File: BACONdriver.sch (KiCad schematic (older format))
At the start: 17 parts, among them P1 Batt_Mon, P2 Batt, P3 Motor, P4 Stearing, U1 ACS712_Mod, U2 VNH2SP30, U3 ACS712_Mod, U4 LM358, U5 Metro_Mini

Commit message: Changes to match prototype, adding an nRF24L01 for receiving control commands from the original transmitter and an FTDI style header for future expansion.
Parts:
- added JP1: JUMPER, Pin_Headers:Pin_Header_Straight_1x02, symbol JUMPER
- added P5: FTDI, Pin_Headers:Pin_Header_Straight_1x06, symbol CONN_01X06
- added U7: nRF24L01+, Pin_Headers:Pin_Header_Straight_2x04, symbol nRF24L01+
- P1: footprint (none) -> Pin_Headers:Pin_Header_Straight_1x04
- P2, P3: footprint (none) -> Pin_Headers:Pin_Header_Straight_1x02
- P4: footprint (none) -> Pin_Headers:Pin_Header_Straight_1x03; symbol CONN_01X05 -> CONN_01X03
- R1, R2, R3, R4, R5, R6, R7, R8: footprint (none) -> Resistors_ThroughHole:Resistor_Horizontal_RM10mm
- U1, U3: footprint (none) -> Pin_Headers:Pin_Header_Straight_1x03
- U2: footprint (none) -> Pin_Headers:Pin_Header_Straight_1x07
- U4: footprint (none) -> Housings_DIP:DIP-8_W7.62mm; symbol LM358 -> LM358-RESCUE-BACONdriver
- U5: footprint (none) -> BACONdriver:MetroMini
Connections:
- net labels added: +3V3, CTS, MISO, MOSI, NRF_CS, NRF_ENABLE, NRF_IRQ, RTS, RXD, SCK, STEAR, TXD
- net labels removed: +3.3V, PWD
- wire segments 49 -> 76
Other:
- moved on the sheet: U2

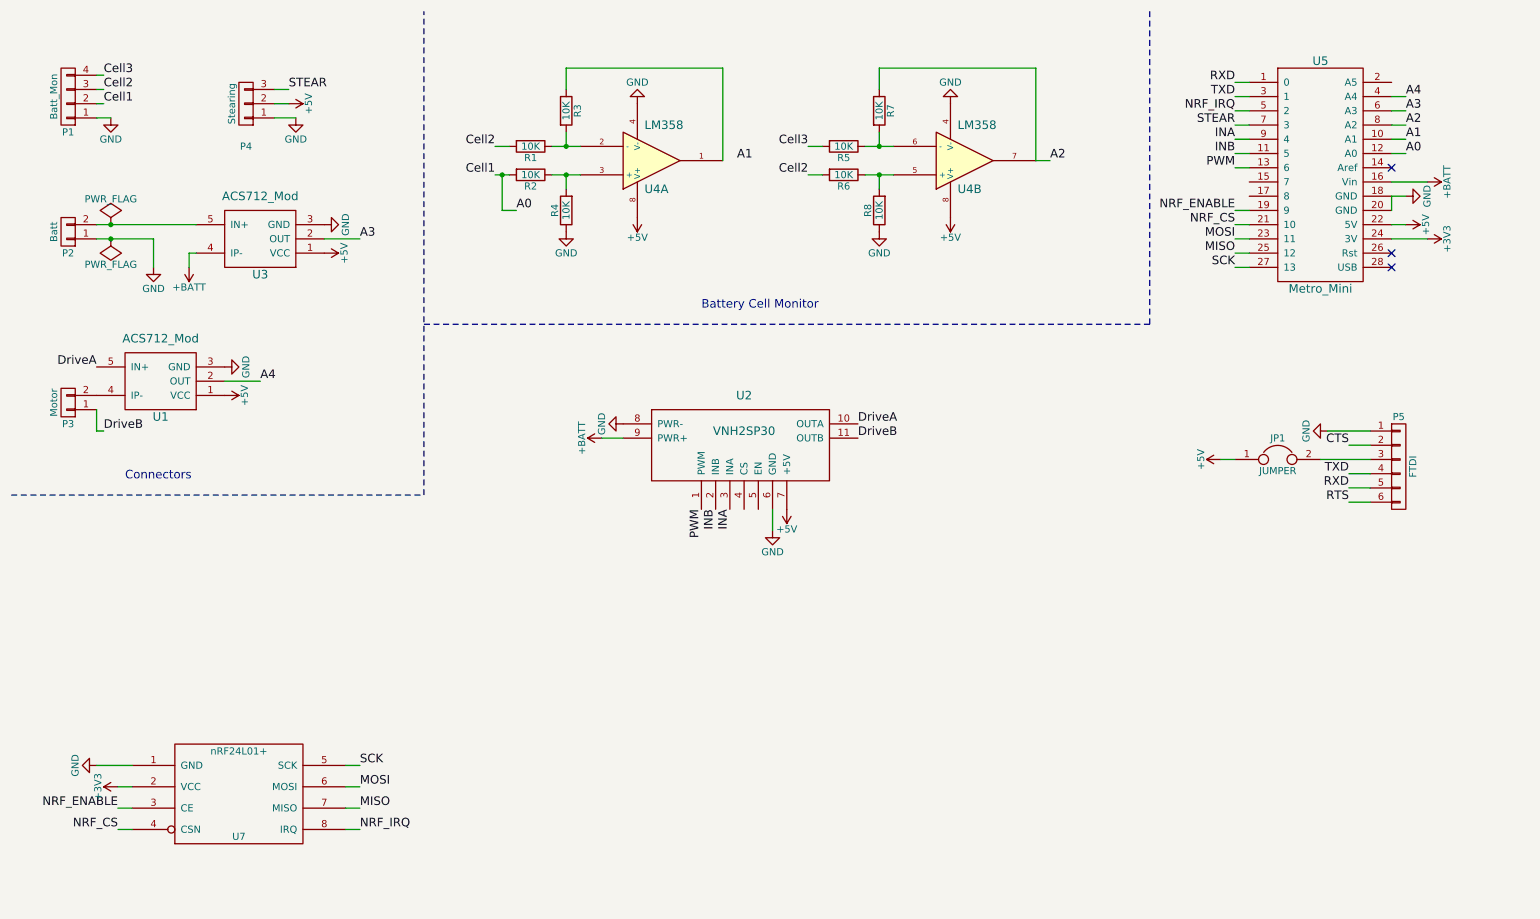
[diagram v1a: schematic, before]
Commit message: Various updates;  - Break out spare pins  - Use the motor driver CS for motor current (Current Sense not Chip Select)  - Allow the FTDI Vcc to be switched between 3.3v and 5v
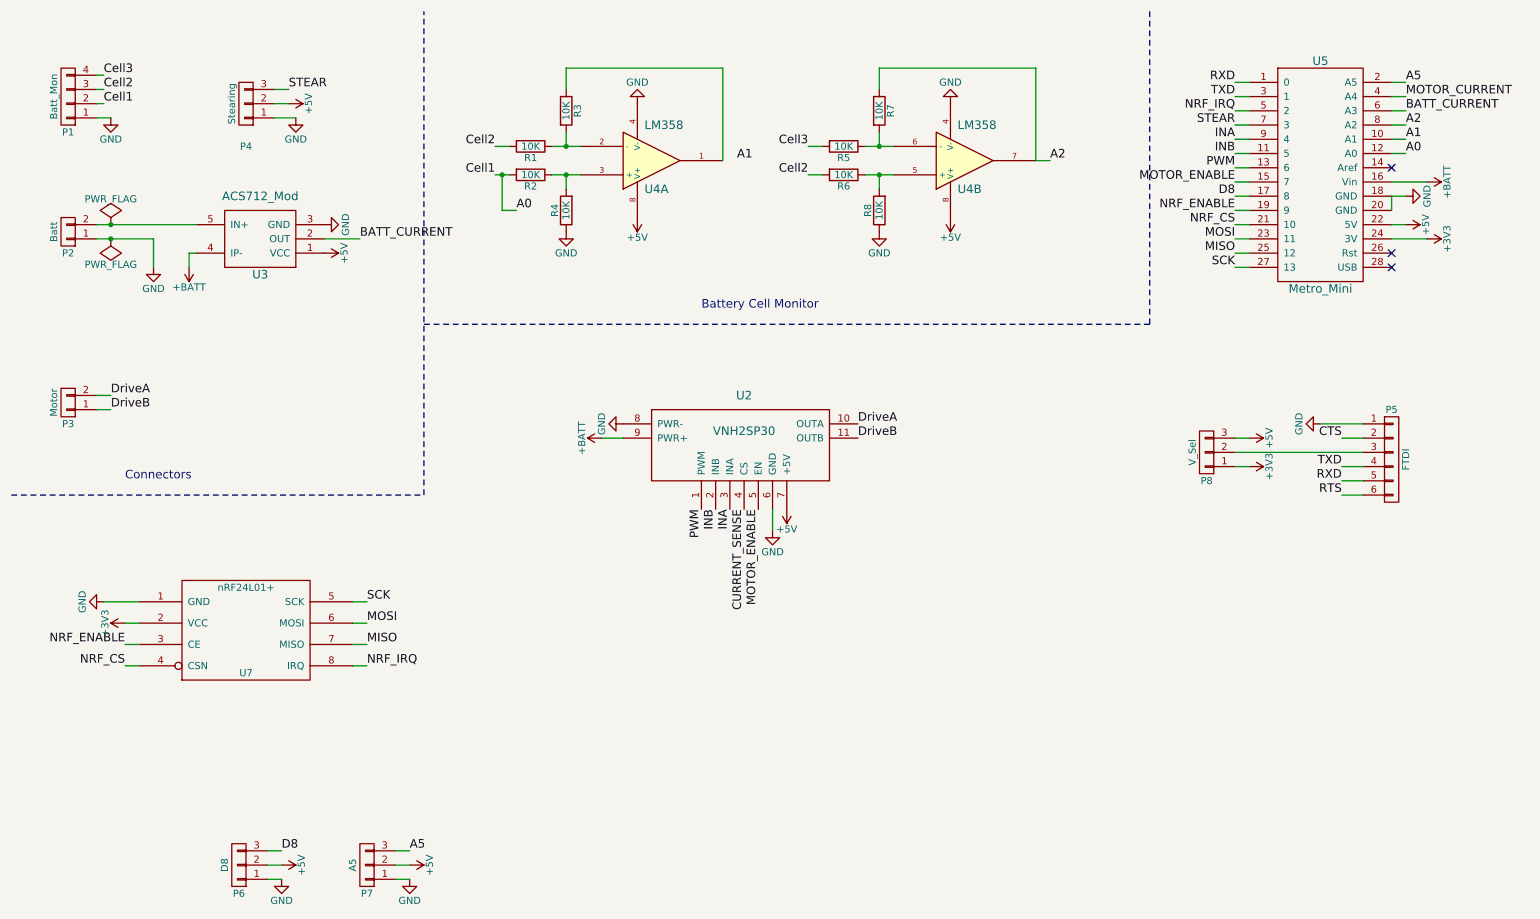
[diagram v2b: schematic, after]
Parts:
- removed JP1: JUMPER, Pin_Headers:Pin_Header_Straight_1x02, symbol JUMPER
- removed U1: ACS712_Mod, Pin_Headers:Pin_Header_Straight_1x03, symbol ACS712_Mod
- added P6: D8, Pin_Headers:Pin_Header_Straight_1x03, symbol CONN_01X03
- added P7: A5, Pin_Headers:Pin_Header_Straight_1x03, symbol CONN_01X03
- added P8: V_Sel, Pin_Headers:Pin_Header_Straight_1x03, symbol CONN_01X03
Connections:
- net +3V3: now also P8.1 (P1)
- net +5V: now also P6.2 (P2), P7.2 (P2), P8.3 (P3)
- net DriveA: now also P3.2 (P2)
- net GND: now also P6.1 (P1), P7.1 (P1)
- net MOTOR_ENABLE: now reaches U5.15 (7)
- net MOTOR_ENABLE: now also U2.5 (EN)
- net D8: now reaches U5.17 (8)
- net D8: now also P6.3 (P3)
- net A5: now reaches U5.2 (A5)
- net A5: now also P7.3 (P3)
- net CURRENT_SENSE: now reaches U2.4 (CS)
- net at P5.3 (P3): now also P8.2 (P2)
- net A3 renamed BATT_CURRENT
- net A4 renamed MOTOR_CURRENT
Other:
- moved on the sheet: P5, U7

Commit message: Moved the components that need laying out to a sub-sheet so the net list can be generated for just those components, while also maintaining the high level wiring
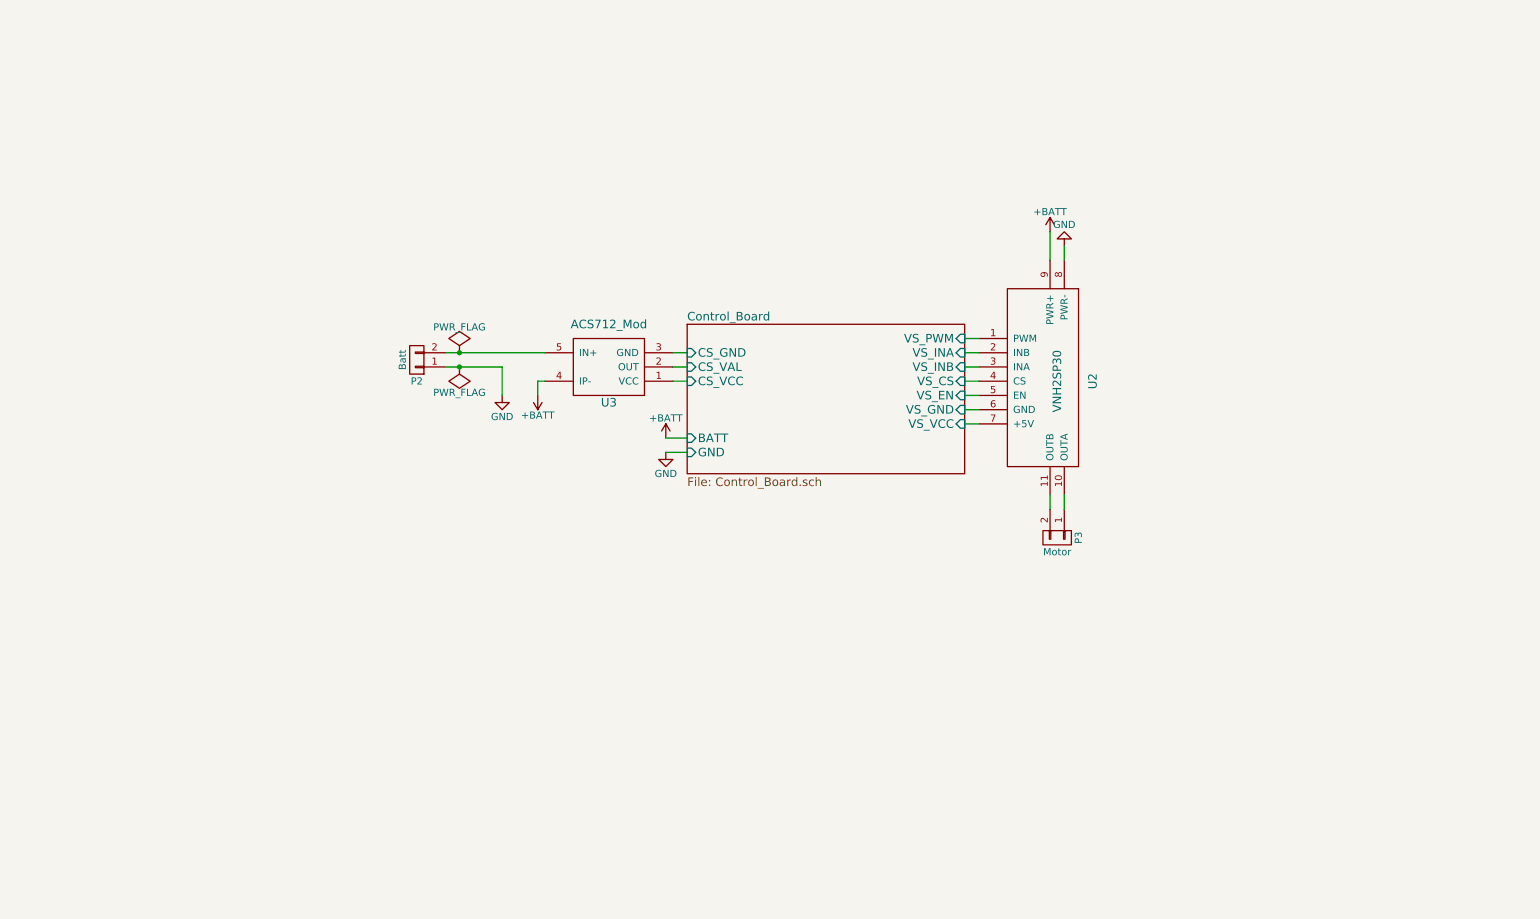
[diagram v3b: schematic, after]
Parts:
- removed P1: Batt_Mon, Pin_Headers:Pin_Header_Straight_1x04, symbol CONN_01X04
- removed P4: Stearing, Pin_Headers:Pin_Header_Straight_1x03, symbol CONN_01X03
- removed P5: FTDI, Pin_Headers:Pin_Header_Straight_1x06, symbol CONN_01X06
- removed P6: D8, Pin_Headers:Pin_Header_Straight_1x03, symbol CONN_01X03
- removed P7: A5, Pin_Headers:Pin_Header_Straight_1x03, symbol CONN_01X03
- removed P8: V_Sel, Pin_Headers:Pin_Header_Straight_1x03, symbol CONN_01X03
- removed R1, R2, R3, R4, R5, R6, R7, R8: 10K, Resistors_ThroughHole:Resistor_Horizontal_RM10mm, symbol R
- removed U4: LM358, Housings_DIP:DIP-8_W7.62mm, symbol LM358-RESCUE-BACONdriver
- removed U5: Metro_Mini, BACONdriver:MetroMini, symbol Metro_Mini
- removed U7: nRF24L01+, Pin_Headers:Pin_Header_Straight_2x04, symbol nRF24L01+
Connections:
- net GND: no longer U2.6 (GND), U3.3 (GND)
- net +5V renamed Control_Board/CS_VCC
- net Control_Board/CS_VCC: no longer U2.7 (+5V)
- net BATT_CURRENT renamed Control_Board/CS_VAL
- net CURRENT_SENSE renamed Control_Board/VS_CS
- net DriveA: no longer names the net of U2.10 (OUTA)
- net DriveA: now also P3.1 (P1); no longer P3.2 (P2)
- net DriveB: no longer names the net of U2.11 (OUTB)
- net DriveB: now also P3.2 (P2); no longer P3.1 (P1)
- net INA renamed Control_Board/VS_INB
- net INB renamed Control_Board/VS_INA
- net MOTOR_ENABLE renamed Control_Board/VS_EN
- net PWM renamed Control_Board/VS_PWM
- new net Control_Board/CS_GND: U3.3 (GND)
- new net Control_Board/VS_GND: U2.6 (GND)
- new net Control_Board/VS_VCC: U2.7 (+5V)
- no-connect marks 3 -> 0
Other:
- note removed: "Battery Cell Monitor"
- note removed: "Connectors"
- moved on the sheet: P2, P3, U2, U3

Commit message: Initial layout of the control board to get positioning for making up on some prototyping board.
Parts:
- P2, P3: footprint Pin_Headers:Pin_Header_Straight_1x02 -> (none)
- U2: footprint Pin_Headers:Pin_Header_Straight_1x07 -> (none)
- U3: footprint Pin_Headers:Pin_Header_Straight_1x03 -> (none)
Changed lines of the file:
@@
 F 0 "P2" H 3350 3100 50  0000 C CNN
 F 1 "Batt" V 3450 2950 50  0000 C CNN
-F 2 "Pin_Headers:Pin_Header_Straight_1x02" H 3350 2950 60  0001 C CNN
+F 2 "" H 3350 2950 60  0001 C CNN
 F 3 "" H 3350 2950 60  0000 C CNN
 	1    3350 2950
@@
 $EndComp
 $Comp
-L GND #PWR1
+L GND #PWR01
 U 1 1 561F01FA
 P 3950 3200
-F 0 "#PWR1" H 3950 2950 50  0001 C CNN
+F 0 "#PWR01" H 3950 2950 50  0001 C CNN
 F 1 "GND" H 3950 3050 50  0000 C CNN
 F 2 "" H 3950 3200 60  0000 C CNN
@@
 $EndComp
 $Comp
-L +BATT #PWR2
+L +BATT #PWR02
 U 1 1 561F0240
 P 4200 3200
-F 0 "#PWR2" H 4200 3050 50  0001 C CNN
+F 0 "#PWR02" H 4200 3050 50  0001 C CNN
 F 1 "+BATT" H 4200 3340 50  0000 C CNN
 F 2 "" H 4200 3200 60  0000 C CNN
@@
 $EndComp
 $Comp
-L PWR_FLAG #FLG1
+L PWR_FLAG #FLG03
 U 1 1 561F0278
 P 3650 2900
-F 0 "#FLG1" H 3650 2995 50  0001 C CNN
+F 0 "#FLG03" H 3650 2995 50  0001 C CNN
 F 1 "PWR_FLAG" H 3650 3080 50  0000 C CNN
 F 2 "" H 3650 2900 60  0000 C CNN
@@
 $EndComp
 $Comp
-L PWR_FLAG #FLG2
+L PWR_FLAG #FLG04
 U 1 1 561F0292
 P 3650 3000
-F 0 "#FLG2" H 3650 3095 50  0001 C CNN
+F 0 "#FLG04" H 3650 3095 50  0001 C CNN
 F 1 "PWR_FLAG" H 3650 3180 50  0000 C CNN
 F 2 "" H 3650 3000 60  0000 C CNN
@@
 F 0 "U3" H 4700 3250 60  0000 C CNN
 F 1 "ACS712_Mod" H 4700 2700 60  0000 C CNN
-F 2 "Pin_Headers:Pin_Header_Straight_1x03" H 4750 3000 60  0001 C CNN
+F 2 "" H 4750 3000 60  0001 C CNN
 F 3 "" H 4750 3000 60  0000 C CNN
 	1    4700 3000
@@
 F 0 "U2" H 7800 3400 60  0000 C CNN
 F 1 "VNH2SP30" H 7800 3150 60  0000 C CNN
-F 2 "Pin_Headers:Pin_Header_Straight_1x07" H 7800 3100 60  0001 C CNN
+F 2 "" H 7800 3100 60  0001 C CNN
 F 3 "" H 7800 3100 60  0000 C CNN
 	1    7800 3100
@@
 F 0 "P3" H 7850 4350 50  0000 C CNN
 F 1 "Motor" V 7950 4200 50  0000 C CNN
-F 2 "Pin_Headers:Pin_Header_Straight_1x02" H 7850 4200 60  0001 C CNN
+F 2 "" H 7850 4200 60  0001 C CNN
 F 3 "" H 7850 4200 60  0000 C CNN
 	1    7850 4200
@@
 $EndComp
 $Comp
-L GND #PWR6
+L GND #PWR05
 U 1 1 561F737B
 P 5100 3600
-F 0 "#PWR6" H 5100 3350 50  0001 C CNN
+F 0 "#PWR05" H 5100 3350 50  0001 C CNN
 F 1 "GND" H 5100 3450 50  0000 C CNN
 F 2 "" H 5100 3600 60  0000 C CNN
@@
 $EndComp
 $Comp
-L +BATT #PWR5
+L +BATT #PWR06
 U 1 1 561F7979
 P 5100 3500
-F 0 "#PWR5" H 5100 3350 50  0001 C CNN
+F 0 "#PWR06" H 5100 3350 50  0001 C CNN
 F 1 "+BATT" H 5100 3640 50  0000 C CNN
 F 2 "" H 5100 3500 60  0000 C CNN
@@
 	3550 2900 4250 2900
 $Comp
-L GND #PWR?
+L GND #PWR07
 U 1 1 56BCF0C0
 P 7900 2150
-F 0 "#PWR?" H 7900 1900 50  0001 C CNN
+F 0 "#PWR07" H 7900 1900 50  0001 C CNN
 F 1 "GND" H 7900 2000 50  0000 C CNN
 F 2 "" H 7900 2150 60  0000 C CNN
@@
 $EndComp
 $Comp
-L +BATT #PWR?
+L +BATT #PWR08
 U 1 1 56BCF0C6
 P 7800 2050
-F 0 "#PWR?" H 7800 1900 50  0001 C CNN
+F 0 "#PWR08" H 7800 1900 50  0001 C CNN
 F 1 "+BATT" H 7800 2190 50  0000 C CNN
 F 2 "" H 7800 2050 60  0000 C CNN
